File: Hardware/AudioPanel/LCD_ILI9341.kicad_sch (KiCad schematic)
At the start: 2 parts, among them U1 CR2013-MI2120

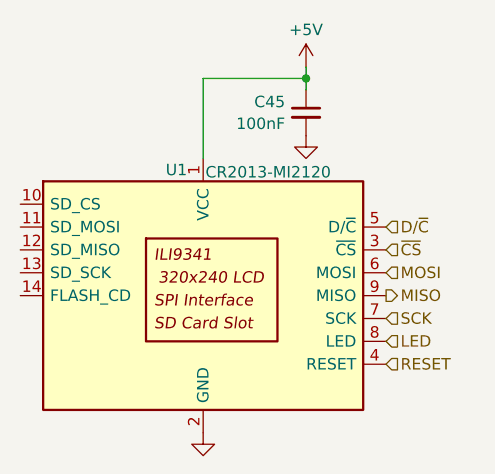
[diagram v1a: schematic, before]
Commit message: Added headphone and speaker jack interfaces
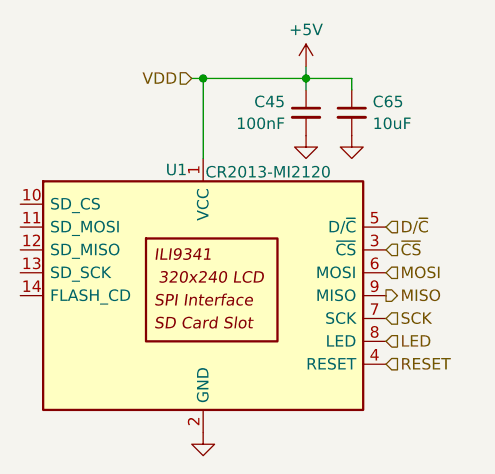
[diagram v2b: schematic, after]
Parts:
- added C65: 10uF, symbol Device:C_Small
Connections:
- net +5V: now also C65.1
- net GND: now also C65.2
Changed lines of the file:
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@@
 	(paper "A4")
+	(junction
+		(at 149.86 77.47)
+		(diameter 0)
+		(color 0 0 0 0)
+	)
 	(junction
 		(at 161.29 77.47)
@@
 	(wire
 		(pts
-			(xy 161.29 77.47) (xy 161.29 78.74)
+			(xy 166.37 77.47) (xy 161.29 77.47)
 		)
 		(stroke
@@
 	(wire
 		(pts
-			(xy 161.29 76.2) (xy 161.29 77.47)
+			(xy 166.37 78.74) (xy 166.37 77.47)
 		)
 		(stroke
@@
 	(wire
 		(pts
-			(xy 149.86 77.47) (xy 161.29 77.47)
+			(xy 161.29 77.47) (xy 161.29 78.74)
 		)
 		(stroke
@@
 		)
 	)
+	(wire
+		(pts
+			(xy 161.29 76.2) (xy 161.29 77.47)
+		)
+		(stroke
+			(width 0)
+			(type default)
+		)
+	)
+	(wire
+		(pts
+			(xy 149.86 77.47) (xy 161.29 77.47)
+		)
+		(stroke
+			(width 0)
+			(type default)
+		)
+	)
+	(wire
+		(pts
+			(xy 148.59 77.47) (xy 149.86 77.47)
+		)
+		(stroke
+			(width 0)
+			(type default)
+		)
+	)
 	(hierarchical_label "MOSI"
 		(shape input)
@@
 			)
 			(justify left)
+		)
+	)
+	(hierarchical_label "VDD"
+		(shape input)
+		(at 148.59 77.47 180)
+		(effects
+			(font
+				(size 1.27 1.27)
+			)
+			(justify right)
 		)
 	)
@@
 	(symbol
 		(lib_id "power:GND")
+		(at 166.37 83.82 0)
+		(unit 1)
+		(exclude_from_sim no)
+		(in_bom yes)
+		(on_board yes)
+		(dnp no)
+		(fields_autoplaced yes)
+		(property "Reference" "#PWR0175"
+			(at 166.37 90.17 0)
+			(effects
+				(font
+					(size 1.27 1.27)
+				)
+				(hide yes)
+			)
+		)
+		(property "Value" "GND"
+			(at 166.37 87.9531 0)
+			(effects
+				(font
+					(size 1.27 1.27)
+				)
+				(hide yes)
+			)
+		)
+		(property "Footprint" ""
+			(at 166.37 83.82 0)
+			(effects
+				(font
+					(size 1.27 1.27)
+				)
+				(hide yes)
+			)
+		)
+		(property "Datasheet" ""
+			(at 166.37 83.82 0)
+			(effects
+				(font
+					(size 1.27 1.27)
+				)
+				(hide yes)
+			)
+		)
+		(property "Description" "Power symbol creates a global label with name \"GND\" , ground"
+			(at 166.37 83.82 0)
+			(effects
+				(font
+					(size 1.27 1.27)
+				)
+				(hide yes)
+			)
+		)
+		(pin "1"
+		)
+		(instances
+			(project "PilotAudioPanel"
+				(path "/2de36a1b-eee5-458c-8325-256a7162eff5/a5cce8a2-fa1f-45df-8605-c295d18be7f1/8cd98acd-8181-4de8-8643-8b9e6d1d3a2e"
+					(reference "#PWR0175")
+					(unit 1)
+				)
+			)
+		)
+	)
+	(symbol
+		(lib_id "power:GND")
 		(at 161.29 83.82 0)
 		(unit 1)
@@
 					(unit 1)
 				)
+			)
+		)
+	)
+	(symbol
+		(lib_id "Device:C_Small")
+		(at 166.37 81.28 0)
+		(unit 1)
+		(exclude_from_sim no)
+		(in_bom yes)
+		(on_board yes)
+		(dnp no)
+		(property "Reference" "C65"
+			(at 168.6941 80.0741 0)
+			(effects
+				(font
+					(size 1.27 1.27)
+				)
+				(justify left)
+			)
+		)
+		(property "Value" "10uF"
+			(at 168.6941 82.4984 0)
+			(effects
+				(font
+					(size 1.27 1.27)
+				)
+				(justify left)
+			)
+		)
+		(property "Footprint" ""
+			(at 166.37 81.28 0)
+			(effects
+				(font
+					(size 1.27 1.27)
+				)
+				(hide yes)
+			)
+		)
+		(property "Datasheet" "~"
+			(at 166.37 81.28 0)
+			(effects
+				(font
+					(size 1.27 1.27)
+				)
+				(hide yes)
+			)
+		)
+		(property "Description" "Unpolarized capacitor, small symbol"
+			(at 166.37 81.28 0)
+			(effects
+				(font
+					(size 1.27 1.27)
+				)
+				(hide yes)
+			)
+		)
+		(pin "1"
+		)
+		(pin "2"
+		)
+		(instances
+			(project "PilotAudioPanel"
+				(path "/2de36a1b-eee5-458c-8325-256a7162eff5/a5cce8a2-fa1f-45df-8605-c295d18be7f1/8cd98acd-8181-4de8-8643-8b9e6d1d3a2e"
+					(reference "C65")
+					(unit 1)
+				)

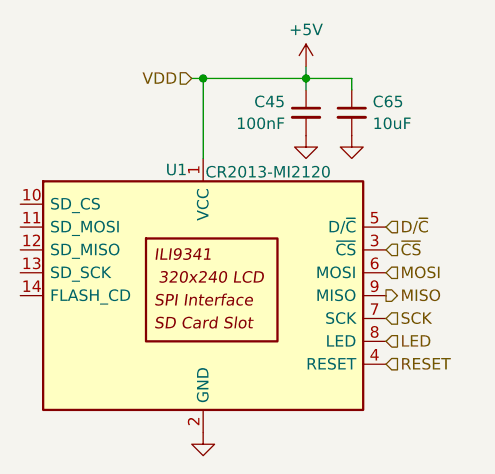
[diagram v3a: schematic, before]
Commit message: Realized that I need to rethink how I'm going to mix the radio audio with the stereo audio
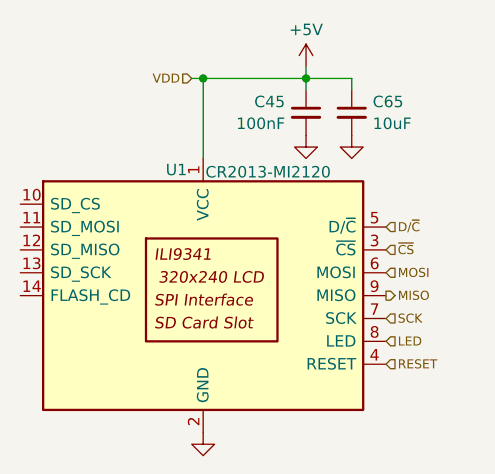
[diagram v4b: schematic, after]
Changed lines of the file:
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@@
 		(effects
 			(font
-				(size 1.27 1.27)
+				(size 1 1)
 				(color 105 14 0 1)
 			)
@@
 		(effects
 			(font
-				(size 1.27 1.27)
+				(size 1 1)
 				(color 105 14 0 1)
 			)
@@
 		(effects
 			(font
-				(size 1.27 1.27)
+				(size 1 1)
 			)
 			(justify right)
@@
 		(effects
 			(font
-				(size 1.27 1.27)
+				(size 1 1)
 				(color 105 14 0 1)
 			)
@@
 		(effects
 			(font
-				(size 1.27 1.27)
+				(size 1 1)
 				(color 105 14 0 1)
 			)
@@
 		(effects
 			(font
-				(size 1.27 1.27)
+				(size 1 1)
 				(color 105 14 0 1)
 			)
@@
 		(effects
 			(font
-				(size 1.27 1.27)
+				(size 1 1)
 				(color 105 14 0 1)
 			)
@@
 		(effects
 			(font
-				(size 1.27 1.27)
+				(size 1 1)
 				(color 105 14 0 1)
 			)
